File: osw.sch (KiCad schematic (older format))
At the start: 56 parts, among them J1 Conn_01x02, J2 Conn_01x04, J3 Conn_01x02, Q1 2N7002, SW1 SW_Push, SW2 SW_Push, SW4 SW_Push, SW5 SW_Push, U1 DS3231MZ, U10 LTC3440EMS, U11 MCP73831T-2ACI_OT, U2 BMA400, U3 BMP280, U4 GC9A01_IPS_display, U5 USB-OTG, U6 CH340E, U7 ttgo-32-micro, U8 Quectel_L96, U9 TPS2115A

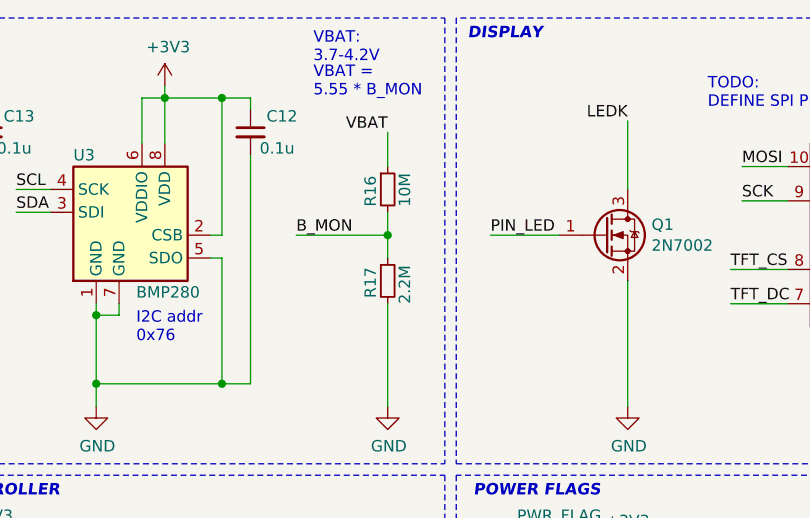
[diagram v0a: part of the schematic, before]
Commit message: update .gitignore, fix battery mon resistors
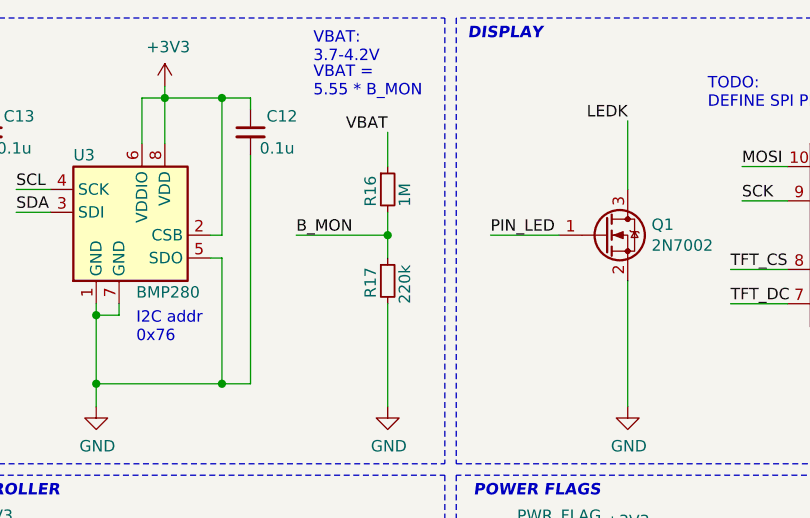
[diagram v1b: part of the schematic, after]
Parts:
- R16: value 10M -> 1M
- R17: value 2.2M -> 220k
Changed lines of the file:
@@
 P 5350 1250
 F 0 "R16" V 5275 1175 50  0000 L CNN
-F 1 "10M" V 5425 1175 50  0000 L CNN
+F 1 "1M" V 5425 1175 50  0000 L CNN
 F 2 "Resistor_SMD:R_0603_1608Metric" H 5350 1250 50  0001 C CNN
 F 3 "~" H 5350 1250 50  0001 C CNN
@@
 P 5350 1650
 F 0 "R17" V 5275 1575 50  0000 L CNN
-F 1 "2.2M" V 5425 1550 50  0000 L CNN
+F 1 "220k" V 5425 1550 50  0000 L CNN
 F 2 "Resistor_SMD:R_0603_1608Metric" H 5350 1650 50  0001 C CNN
 F 3 "~" H 5350 1650 50  0001 C CNN

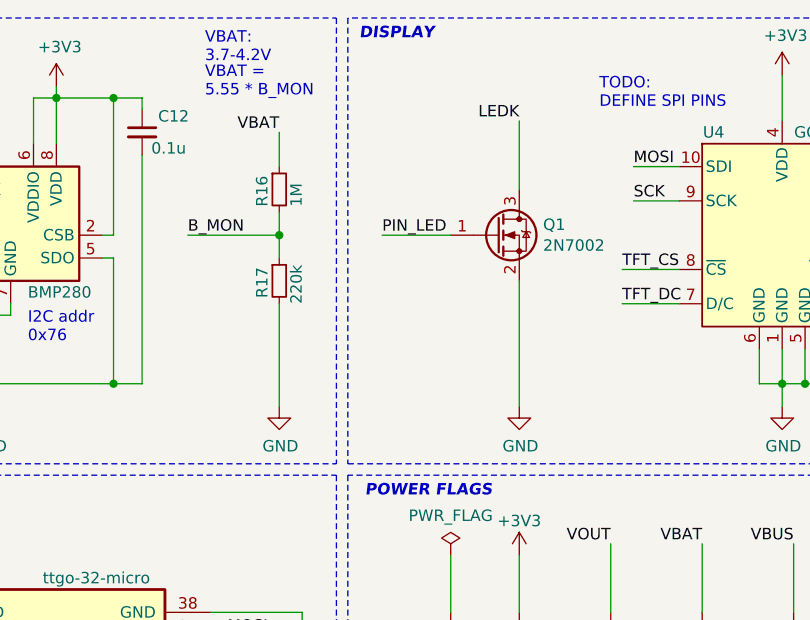
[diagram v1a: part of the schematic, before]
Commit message: add LED FET protection
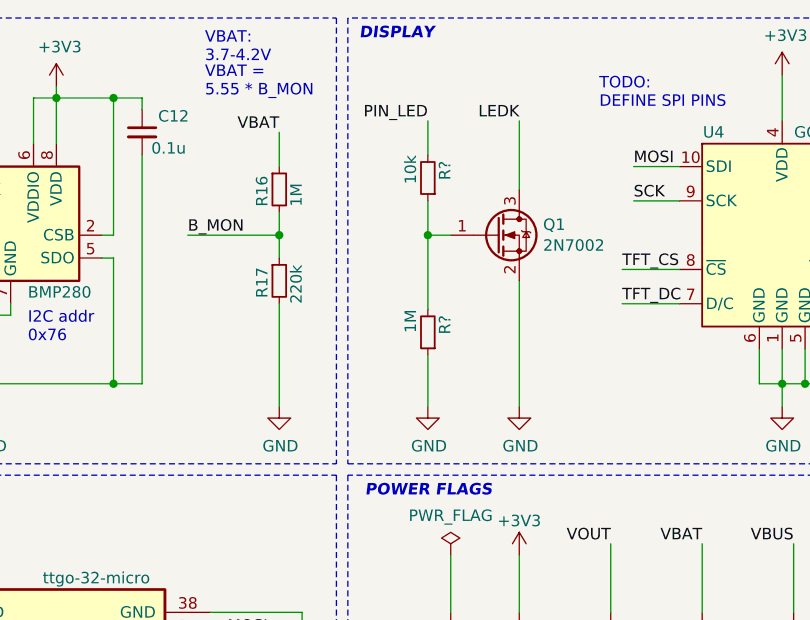
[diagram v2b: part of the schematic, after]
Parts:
- added R?: 10k, Resistor_SMD:R_0603_1608Metric, symbol Device:R_Small
- added R?: 1M, Resistor_SMD:R_0603_1608Metric, symbol Device:R_Small
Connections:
- net GND: now also R?.1
- net PIN_LED: now also R?.2; no longer Q1.1 (G)
- new net: Q1.1 (G), R?.1, R?.2
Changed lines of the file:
@@
 	1    0    0    -1
 $EndComp
-Text Label 5800 1450 0    50   ~ 0
+Text Label 6000 950  2    50   ~ 0
 PIN_LED
 Wire Notes Line
@@
 	8200 4525 8200 5550
 Wire Wire Line
-	5800 1450 6100 1450
+	6000 1450 6100 1450
 Wire Wire Line
 	8400 1250 8400 1300
@@
 Wire Wire Line
 	2750 3325 2750 4125
+$Comp
+L Device:R_Small R?
+U 1 1 5FAF8B20
+P 6000 1200
+F 0 "R?" V 5925 1125 50  0000 L CNN
+F 1 "10k" V 6075 1100 50  0000 L CNN
+F 2 "Resistor_SMD:R_0603_1608Metric" H 6000 1200 50  0001 C CNN
+F 3 "~" H 6000 1200 50  0001 C CNN
+	1    6000 1200
+	-1   0    0    1
+$EndComp
+Wire Wire Line
+	6000 950  6000 1100
+$Comp
+L Device:R_Small R?
+U 1 1 5FC27A03
+P 6000 1875
+F 0 "R?" V 5925 1800 50  0000 L CNN
+F 1 "1M" V 6075 1775 50  0000 L CNN
+F 2 "Resistor_SMD:R_0603_1608Metric" H 6000 1875 50  0001 C CNN
+F 3 "~" H 6000 1875 50  0001 C CNN
+	1    6000 1875
+	-1   0    0    1
+$EndComp
+$Comp
+L power:GND #PWR?
+U 1 1 5FC280D0
+P 6000 2200
+F 0 "#PWR?" H 6000 1950 50  0001 C CNN
+F 1 "GND" H 6005 2027 50  0000 C CNN
+F 2 "" H 6000 2200 50  0001 C CNN
+F 3 "" H 6000 2200 50  0001 C CNN
+	1    6000 2200
+	1    0    0    -1
+$EndComp
+Wire Wire Line
+	6000 2200 6000 1975
+Wire Wire Line
+	6000 1300 6000 1450
+Connection ~ 6000 1450
+Wire Wire Line
+	6000 1450 6000 1775
 $EndSCHEMATC

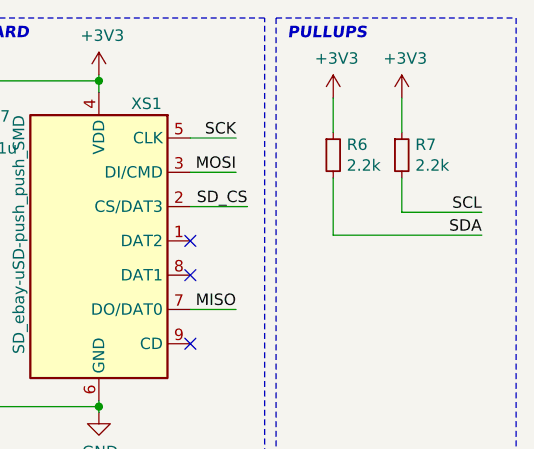
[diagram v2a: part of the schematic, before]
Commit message: set i2c pullups to 1k
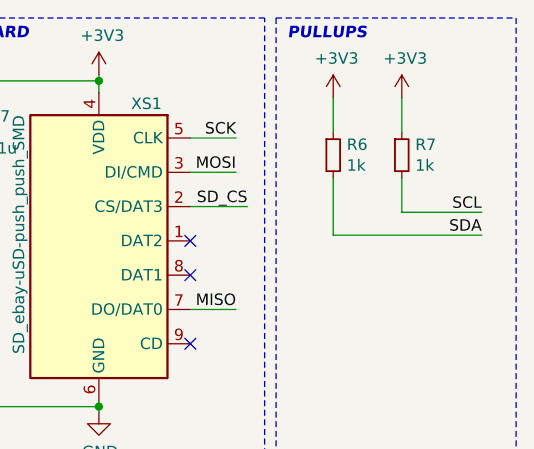
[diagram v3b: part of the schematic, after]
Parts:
- R6, R7: value 2.2k -> 1k
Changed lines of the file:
@@
 P 10300 1100
 F 0 "R6" H 10359 1146 50  0000 L CNN
-F 1 "2.2k" H 10359 1055 50  0000 L CNN
+F 1 "1k" H 10359 1055 50  0000 L CNN
 F 2 "Resistor_SMD:R_0603_1608Metric" H 10300 1100 50  0001 C CNN
 F 3 "~" H 10300 1100 50  0001 C CNN
@@
 P 10600 1100
 F 0 "R7" H 10659 1146 50  0000 L CNN
-F 1 "2.2k" H 10659 1055 50  0000 L CNN
+F 1 "1k" H 10659 1055 50  0000 L CNN
 F 2 "Resistor_SMD:R_0603_1608Metric" H 10600 1100 50  0001 C CNN
 F 3 "~" H 10600 1100 50  0001 C CNN

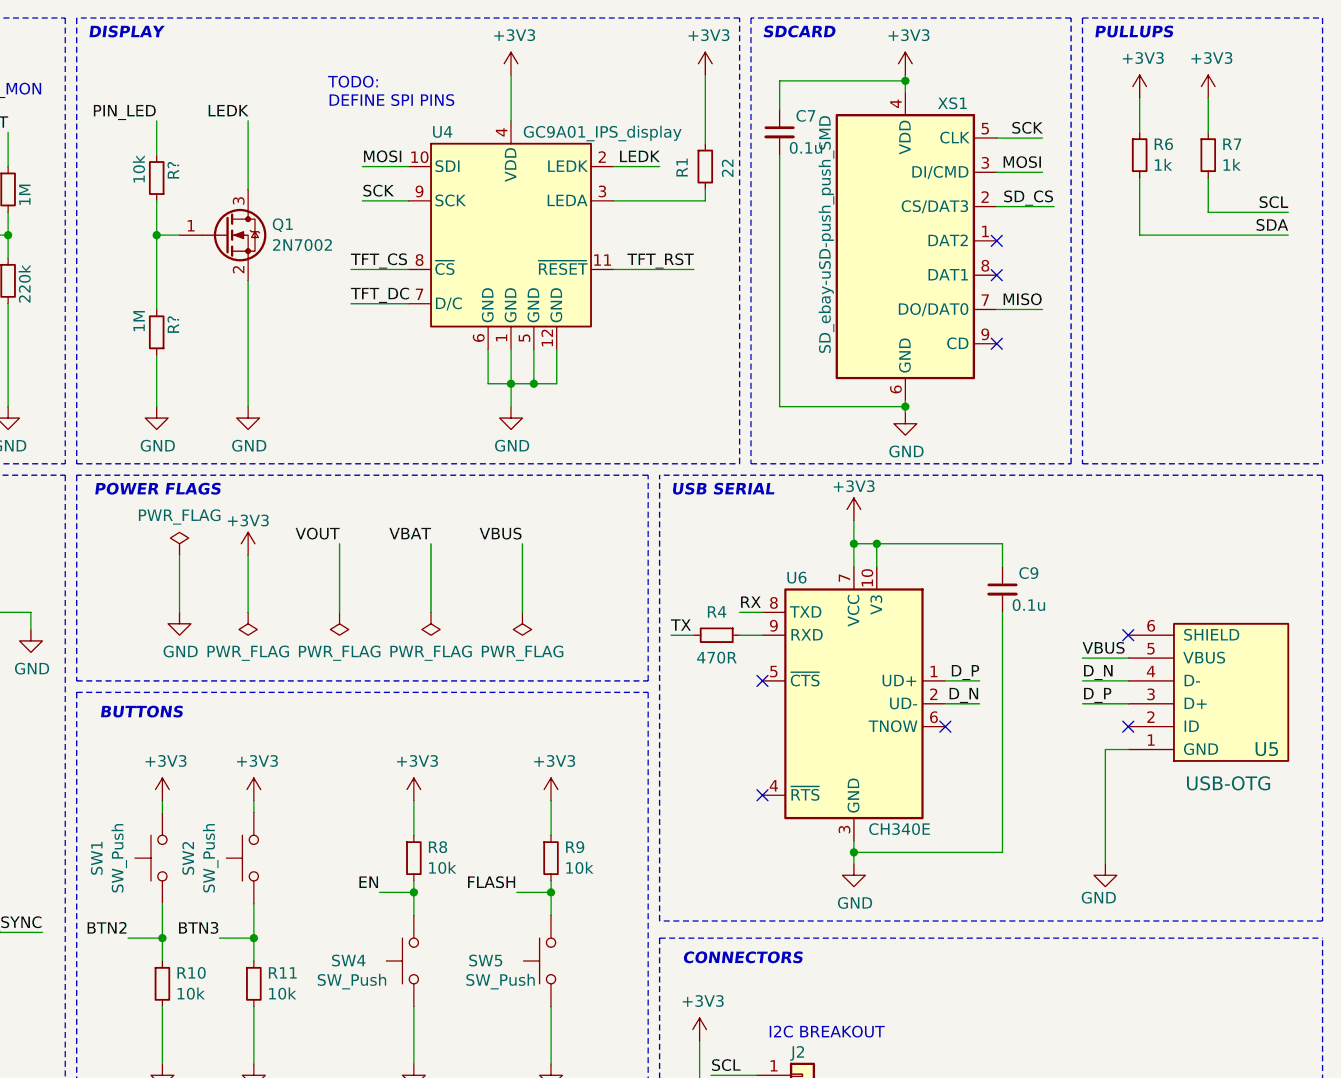
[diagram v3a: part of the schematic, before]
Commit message: add USB protection USBLC6-2SC6
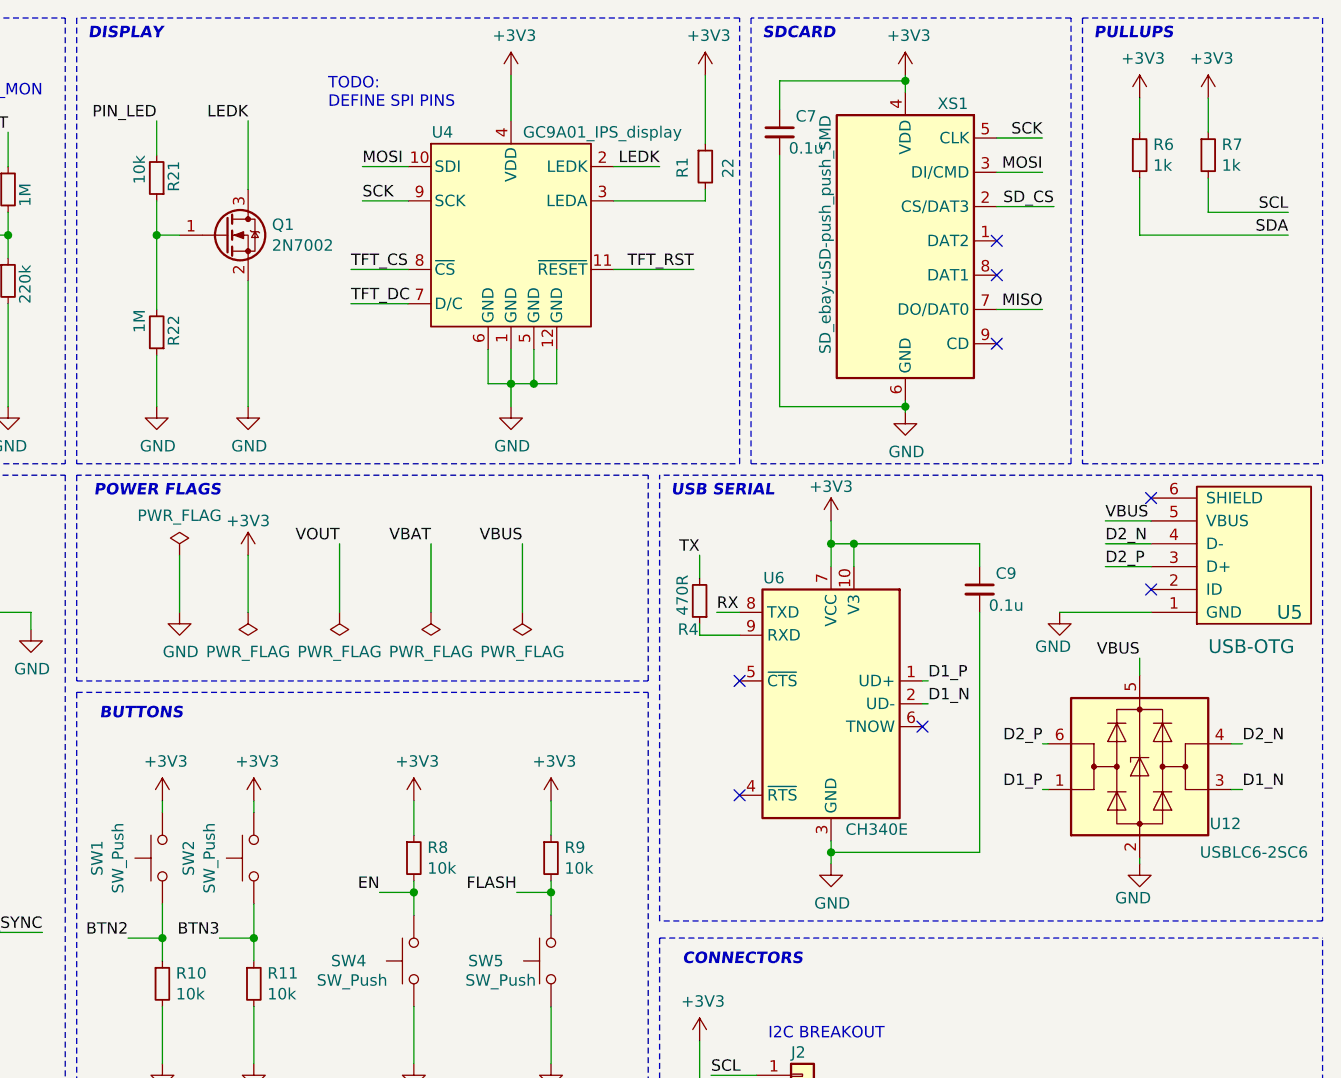
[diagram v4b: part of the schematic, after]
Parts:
- added U12: USBLC6-2SC6, Package_TO_SOT_SMD:SOT-23-6, symbol Power_Protection:USBLC6-2SC6
- gave numbers to parts that had none: 2
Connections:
- net GND: now also U12.2 (GND)
- net VBUS: now also U12.5 (VBUS)
- net D_N renamed D1_N
- net D1_N: now also U12.3 (I/O2); no longer U5.4 (D-)
- net D_P renamed D1_P
- net D1_P: now also U12.1 (I/O1); no longer U5.3 (D+)
- new net D2_N: U12.4 (I/O2), U5.4 (D-)
- new net D2_P: U12.6 (I/O1), U5.3 (D+)
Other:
- moved on the sheet: C9, R4, U5, U6
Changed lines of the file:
@@
 Text Notes 8675 4975 0    50   ~ 0
 I2C BREAKOUT
-Text Label 10050 3300 0    50   ~ 0
+Text Label 10150 2700 0    50   ~ 0
 VBUS
 Wire Wire Line
-	10050 3300 10250 3300
+	10150 2700 10350 2700
 $Comp
 L power:GND #PWR024
 U 1 1 5F56FA17
-P 10150 4200
-F 0 "#PWR024" H 10150 3950 50  0001 C CNN
-F 1 "GND" H 10200 4050 50  0000 R CNN
-F 2 "" H 10150 4200 50  0001 C CNN
-F 3 "" H 10150 4200 50  0001 C CNN
-	1    10150 4200
-	1    0    0    -1
-$EndComp
-Text Label 9600 3500 2    50   ~ 0
-D_N
-Text Label 9600 3400 2    50   ~ 0
-D_P
-Text Label 10050 3400 0    50   ~ 0
-D_N
-Wire Wire Line
-	10050 3500 10250 3500
-Text Label 10050 3500 0    50   ~ 0
-D_P
-Wire Wire Line
-	8550 3200 8650 3200
-Wire Wire Line
-	8250 3200 8350 3200
+P 9950 3100
+F 0 "#PWR024" H 9950 2850 50  0001 C CNN
+F 1 "GND" H 10000 2950 50  0000 R CNN
+F 2 "" H 9950 3100 50  0001 C CNN
+F 3 "" H 9950 3100 50  0001 C CNN
+	1    9950 3100
+	1    0    0    -1
+$EndComp
+Text Label 9375 3500 0    50   ~ 0
+D1_N
+Text Label 9375 3400 0    50   ~ 0
+D1_P
+Text Label 10150 2800 0    50   ~ 0
+D2_N
+Wire Wire Line
+	10150 2900 10350 2900
+Text Label 10150 2900 0    50   ~ 0
+D2_P
+Wire Wire Line
+	8375 2850 8375 2950
 $Comp
 L power:+3V3 #PWR015
 U 1 1 5F56E405
-P 9050 2700
-F 0 "#PWR015" H 9050 2550 50  0001 C CNN
-F 1 "+3V3" H 9050 2850 50  0000 C CNN
-F 2 "" H 9050 2700 50  0001 C CNN
-F 3 "" H 9050 2700 50  0001 C CNN
-	1    9050 2700
-	1    0    0    -1
-$EndComp
-Wire Wire Line
-	9050 4200 9050 4150
+P 8950 2700
+F 0 "#PWR015" H 8950 2550 50  0001 C CNN
+F 1 "+3V3" H 8950 2850 50  0000 C CNN
+F 2 "" H 8950 2700 50  0001 C CNN
+F 3 "" H 8950 2700 50  0001 C CNN
+	1    8950 2700
+	1    0    0    -1
+$EndComp
+Wire Wire Line
+	8950 4200 8950 4150
 $Comp
 L power:GND #PWR025
 U 1 1 5F56CD5A
-P 9050 4200
-F 0 "#PWR025" H 9050 3950 50  0001 C CNN
-F 1 "GND" H 9055 4027 50  0000 C CNN
-F 2 "" H 9050 4200 50  0001 C CNN
-F 3 "" H 9050 4200 50  0001 C CNN
-	1    9050 4200
-	1    0    0    -1
-$EndComp
-Text Label 8250 3200 0    50   ~ 0
+P 8950 4200
+F 0 "#PWR025" H 8950 3950 50  0001 C CNN
+F 1 "GND" H 8955 4027 50  0000 C CNN
+F 2 "" H 8950 4200 50  0001 C CNN
+F 3 "" H 8950 4200 50  0001 C CNN
+	1    8950 4200
+	1    0    0    -1
+$EndComp
+Text Label 8375 2850 2    50   ~ 0
 TX
 Wire Wire Line
-	8550 3100 8650 3100
-Text Label 8550 3100 0    50   ~ 0
+	8450 3100 8550 3100
+Text Label 8450 3100 0    50   ~ 0
 RX
 Wire Wire Line
-	9600 3400 9450 3400
-Wire Wire Line
-	9600 3500 9450 3500
+	9375 3400 9350 3400
+Wire Wire Line
+	9375 3500 9350 3500
 $Comp
 L open-Smartwatch:USB-OTG U5
 U 1 1 5F553576
-P 10500 3300
-F 0 "U5" H 10800 3700 60  0000 L CNN
-F 1 "USB-OTG" H 10500 3850 60  0000 L CNN
-F 2 "open-Smartwatch:USBmicro-B" H 10500 3300 60  0001 C CNN
-F 3 "" H 10500 3300 60  0001 C CNN
-	1    10500 3300
+P 10600 2700
+F 0 "U5" H 10900 3100 60  0000 L CNN
+F 1 "USB-OTG" H 10600 3250 60  0000 L CNN
+F 2 "open-Smartwatch:USBmicro-B" H 10600 2700 60  0001 C CNN
+F 3 "" H 10600 2700 60  0001 C CNN
+	1    10600 2700
 	1    0    0    1
 $EndComp
@@
 	1    0    0    -1
 $EndComp
-NoConn ~ 10250 3600
-NoConn ~ 8650 3900
-Wire Wire Line
-	10250 3400 10050 3400
+NoConn ~ 10350 3000
+NoConn ~ 8550 3900
+Wire Wire Line
+	10350 2800 10150 2800
 NoConn ~ 700  1650
 NoConn ~ 1700 1250
@@
 Wire Wire Line
 	1800 6150 1800 6200
-NoConn ~ 10250 3200
+NoConn ~ 10350 2600
 $Comp
 L open-Smartwatch:CH340E U6
 U 1 1 5F568AB1
-P 9050 3500
-F 0 "U6" H 9300 4050 50  0000 C CNN
-F 1 "CH340E" H 8850 2950 50  0000 C CNN
-F 2 "open-Smartwatch:MSOP-10_3x3mm_P0.5mm" H 9100 2950 50  0001 L CNN
-F 3 "https://www.mpja.com/download/35227cpdata.pdf" H 8700 4300 50  0001 C CNN
-	1    9050 3500
+P 8950 3500
+F 0 "U6" H 9200 4050 50  0000 C CNN
+F 1 "CH340E" H 8750 2950 50  0000 C CNN
+F 2 "open-Smartwatch:MSOP-10_3x3mm_P0.5mm" H 9000 2950 50  0001 L CNN
+F 3 "https://www.mpja.com/download/35227cpdata.pdf" H 8600 4300 50  0001 C CNN
+	1    8950 3500
 	-1   0    0    -1
 $EndComp
-NoConn ~ 9450 3600
-NoConn ~ 8650 3400
-Wire Wire Line
-	9050 2700 9050 2800
-Wire Wire Line
-	9050 2800 9150 2800
-Wire Wire Line
-	9150 2800 9150 2900
-Connection ~ 9050 2800
+NoConn ~ 9350 3600
+NoConn ~ 8550 3400
+Wire Wire Line
+	8950 2700 8950 2800
+Wire Wire Line
+	8950 2800 9050 2800
 Wire Wire Line
 	9050 2800 9050 2900
+Connection ~ 8950 2800
+Wire Wire Line
+	8950 2800 8950 2900
 Wire Notes Line
 	3050 5500 500  5500
@@
 Text Label 10950 1350 2    50   ~ 0
 SCL
-Wire Wire Line
-	10250 3700 10150 3700
-Wire Wire Line
-	10150 3700 10150 4200
 Wire Notes Line
 	10050 500  11100 500
@@
 L Device:C_Small C9
 U 1 1 5F753E14
-P 9700 3000
-F 0 "C9" H 9770 3070 50  0000 L CNN
-F 1 "0.1u" H 9740 2930 50  0000 L CNN
-F 2 "Capacitor_SMD:C_0603_1608Metric" H 9700 3000 50  0001 C CNN
-F 3 "~" H 9700 3000 50  0001 C CNN
-	1    9700 3000
+P 9600 3000
+F 0 "C9" H 9670 3070 50  0000 L CNN
+F 1 "0.1u" H 9640 2930 50  0000 L CNN
+F 2 "Capacitor_SMD:C_0603_1608Metric" H 9600 3000 50  0001 C CNN
+F 3 "~" H 9600 3000 50  0001 C CNN
+	1    9600 3000
 	1    0    0    -1
 $EndComp
@@
 	5450 7200 6350 7200
 Wire Wire Line
-	9150 2800 9700 2800
-Wire Wire Line
-	9700 2800 9700 2900
-Connection ~ 9150 2800
+	9050 2800 9600 2800
+Wire Wire Line
+	9600 2800 9600 2900
+Connection ~ 9050 2800
 $Comp
 L Device:R_Small R4
 U 1 1 5F5936F4
-P 8450 3200
-F 0 "R4" V 8350 3200 50  0000 C CNN
-F 1 "470R" V 8550 3200 50  0000 C CNN
-F 2 "Resistor_SMD:R_0603_1608Metric" H 8450 3200 50  0001 C CNN
-F 3 "~" H 8450 3200 50  0001 C CNN
-	1    8450 3200
-	0    1    1    0
-$EndComp
-Wire Wire Line
-	9700 3100 9700 4150
-Wire Wire Line
-	9700 4150 9050 4150
-Connection ~ 9050 4150
-Wire Wire Line
-	9050 4150 9050 4100
+P 8375 3050
+F 0 "R4" H 8425 3175 50  0000 C CNN
+F 1 "470R" V 8450 3025 50  0000 C CNN
+F 2 "Resistor_SMD:R_0603_1608Metric" H 8375 3050 50  0001 C CNN
+F 3 "~" H 8375 3050 50  0001 C CNN
+	1    8375 3050
+	-1   0    0    1
+$EndComp
+Wire Wire Line
+	9600 3100 9600 4150
+Wire Wire Line
+	9600 4150 8950 4150
+Connection ~ 8950 4150
+Wire Wire Line
+	8950 4150 8950 4100
 Wire Wire Line
 	1200 800  1200 850
@@
 	2750 3325 2750 4125
 $Comp
-L Device:R_Small R?
+L Device:R_Small R21
 U 1 1 5FAF8B20
 P 6000 1200
-F 0 "R?" V 5925 1125 50  0000 L CNN
+F 0 "R21" V 5925 1125 50  0000 L CNN
 F 1 "10k" V 6075 1100 50  0000 L CNN
 F 2 "Resistor_SMD:R_0603_1608Metric" H 6000 1200 50  0001 C CNN
@@
 	6000 950  6000 1100
 $Comp
-L Device:R_Small R?
+L Device:R_Small R22
 U 1 1 5FC27A03
 P 6000 1875
-F 0 "R?" V 5925 1800 50  0000 L CNN
+F 0 "R22" V 5925 1800 50  0000 L CNN
 F 1 "1M" V 6075 1775 50  0000 L CNN
 F 2 "Resistor_SMD:R_0603_1608Metric" H 6000 1875 50  0001 C CNN
@@
 $EndComp
 $Comp
-L power:GND #PWR?
+L power:GND #PWR0101
 U 1 1 5FC280D0
 P 6000 2200
-F 0 "#PWR?" H 6000 1950 50  0001 C CNN
+F 0 "#PWR0101" H 6000 1950 50  0001 C CNN
 F 1 "GND" H 6005 2027 50  0000 C CNN
 F 2 "" H 6000 2200 50  0001 C CNN
@@
 Wire Wire Line
 	6000 1450 6000 1775
+$Comp
+L Power_Protection:USBLC6-2SC6 U12
+U 1 1 5FCC4A82
+P 10300 3775
+F 0 "U12" H 10675 3525 50  0000 C CNN
+F 1 "USBLC6-2SC6" H 10800 3400 50  0000 C CNN
+F 2 "Package_TO_SOT_SMD:SOT-23-6" H 10300 3275 50  0001 C CNN
+F 3 "https://www.st.com/resource/en/datasheet/usblc6-2.pdf" H 10500 4125 50  0001 C CNN
+	1    10300 3775
+	1    0    0    -1
+$EndComp
+Text Label 10300 3300 2    50   ~ 0
+VBUS
+Wire Wire Line
+	10300 3300 10300 3375
+$Comp
+L power:GND #PWR0102
+U 1 1 5FE3CEB4
+P 10300 4200
+F 0 "#PWR0102" H 10300 3950 50  0001 C CNN
+F 1 "GND" H 10350 4050 50  0000 R CNN
+F 2 "" H 10300 4200 50  0001 C CNN
+F 3 "" H 10300 4200 50  0001 C CNN
+	1    10300 4200
+	1    0    0    -1
+$EndComp
+Wire Wire Line
+	10300 4200 10300 4175
+Text Label 9875 3875 2    50   ~ 0
+D1_P
+Wire Wire Line
+	9875 3875 9900 3875
+Text Label 9875 3675 2    50   ~ 0
+D2_P
+Wire Wire Line
+	9875 3675 9900 3675
+Wire Wire Line
+	8375 3150 8375 3200
+Wire Wire Line
+	8375 3200 8550 3200
+Text Label 10750 3675 0    50   ~ 0
+D2_N
+Wire Wire Line
+	10750 3675 10700 3675
+Text Label 10750 3875 0    50   ~ 0
+D1_N
+Wire Wire Line
+	10700 3875 10750 3875
+Wire Wire Line
+	9950 3100 10350 3100
 $EndSCHEMATC
